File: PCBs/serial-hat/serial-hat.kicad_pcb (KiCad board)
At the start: 2 copper layers, 65 x 56 mm, 21 parts, among them J1 CTS/RTS3, J2 TX/RX3, J3 CTS/RTS2, J4 TX/RX2, J5 UART3, J6 UART2, J7 Conn_02x20_Odd_Even, U1 MAX3232, U2 MAX3232

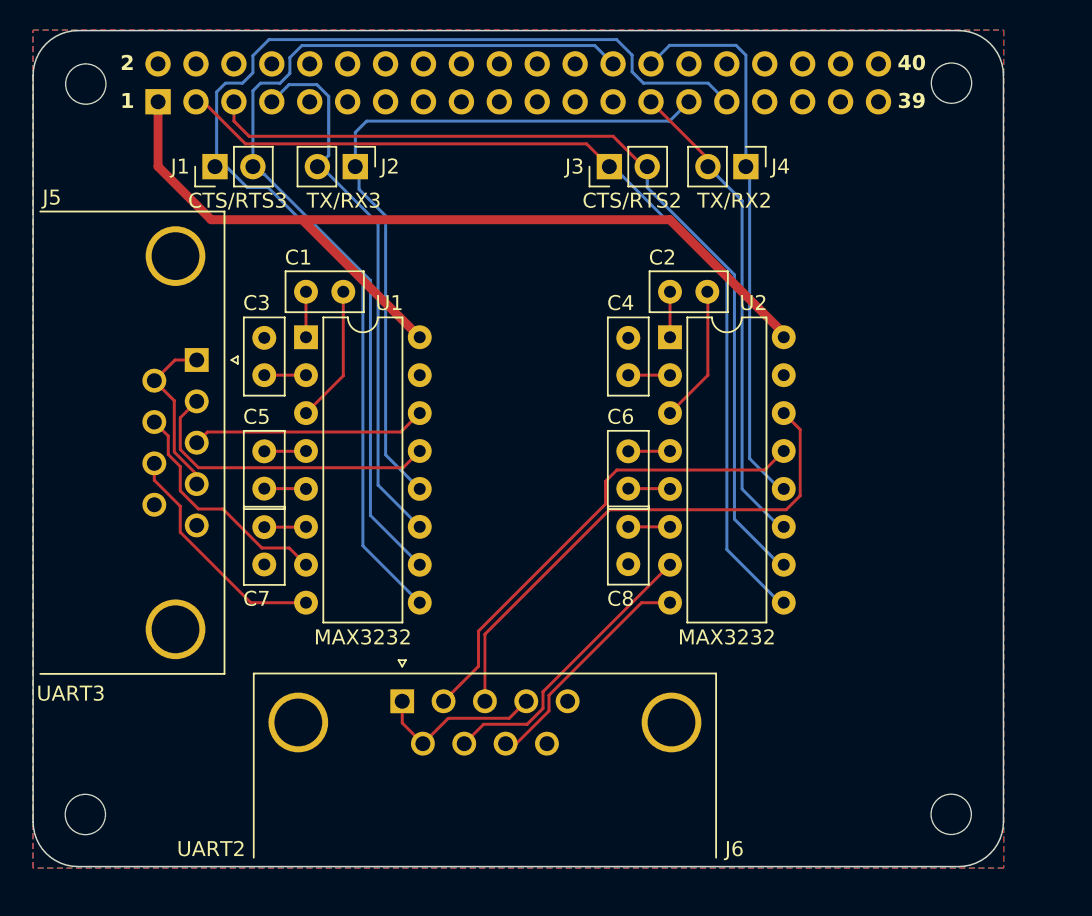
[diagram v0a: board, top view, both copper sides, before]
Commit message: Rework for single MAX3232
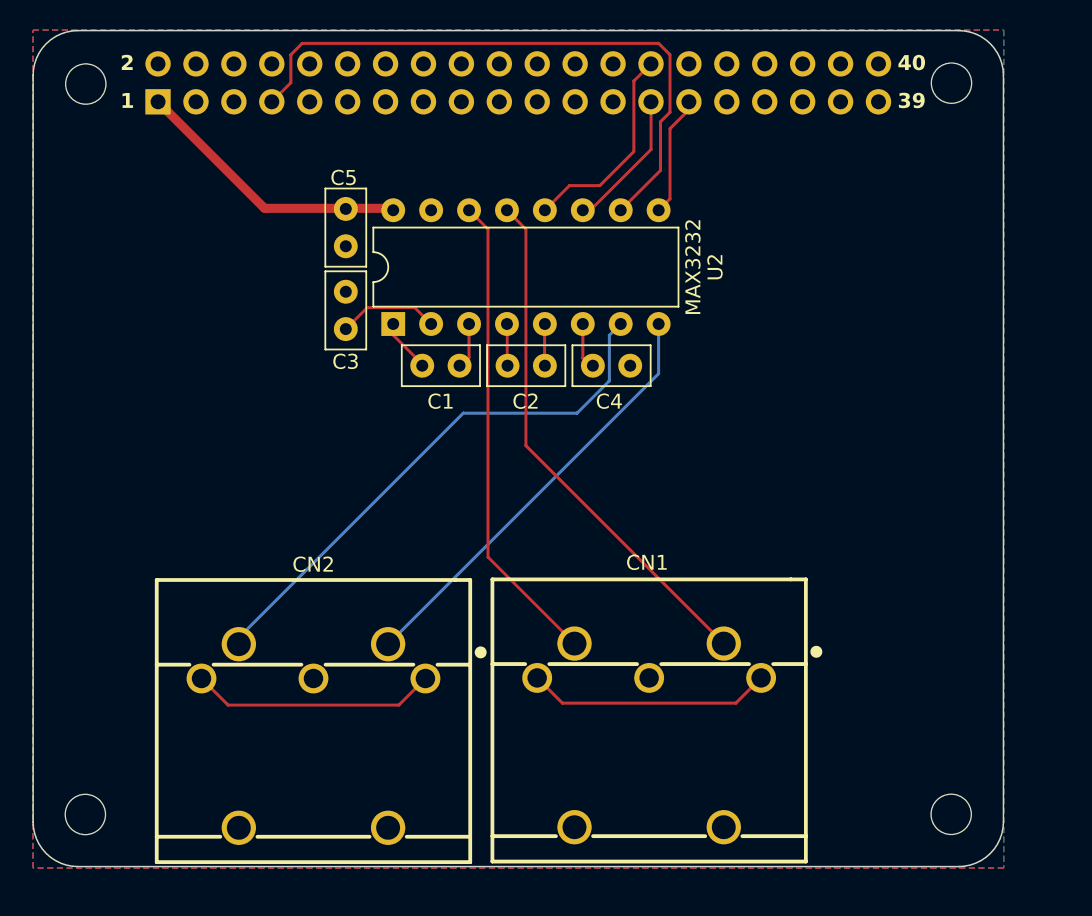
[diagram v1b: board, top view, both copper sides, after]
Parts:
- removed C6, C7, C8: 100nF, Capacitor_THT:C_Disc_D5.0mm_W2.5mm_P2.50mm
- removed J1: CTS/RTS3, Connector_PinHeader_2.54mm:PinHeader_1x02_P2.54mm_Vertical
- removed J2: TX/RX3, Connector_PinHeader_2.54mm:PinHeader_1x02_P2.54mm_Vertical
- removed J3: CTS/RTS2, Connector_PinHeader_2.54mm:PinHeader_1x02_P2.54mm_Vertical
- removed J4: TX/RX2, Connector_PinHeader_2.54mm:PinHeader_1x02_P2.54mm_Vertical
- removed J5: UART3, Connector_Dsub:DSUB-9_Male_Horizontal_P2.77x2.84mm_EdgePinOffset7.70mm_Housed_MountingHolesOffset9.12mm
- removed J6: UART2, Connector_Dsub:DSUB-9_Male_Horizontal_P2.77x2.84mm_EdgePinOffset7.70mm_Housed_MountingHolesOffset9.12mm
- removed U1: MAX3232, Package_DIP:DIP-16_W7.62mm
- added CN1: Modem port, DIN5:CONN-TH_DIN-504-M10, F.Cu at (164.0, 99.8)
- added CN2: Printer port, DIN5:CONN-TH_DIN-504-M10, F.Cu at (141.5, 99.9)
- J7: value Conn_02x20_Odd_Even -> Rpi headers
- moved U2 18.6 mm to (146.8, 72.3), turned to 90 degrees
- moved C5 17.1 mm to (143.6, 64.6)
- moved C2 12.0 mm to (154.5, 75.1)
- moved C1 9.23 mm to (148.8, 75.1)
- moved C3 6.27 mm to (143.6, 72.6)
- moved C4 2.46 mm to (160.2, 75.1), turned to 0 degrees
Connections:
- C1 pad 1: Net-(U1-C1+) -> Net-(U2-C1+)
- C1 pad 2: Net-(U1-C1-) -> Net-(U2-C1-)
- C2 pad 1: Net-(U2-C1+) -> Net-(U2-C2+)
- C2 pad 2: Net-(U2-C1-) -> Net-(U2-C2-)
- C3 pad 1: Net-(U1-VS+) -> Net-(U2-VS+)
- C4 pad 1: Net-(U2-VS+) -> Net-(U2-VS-)
- C5 pad 1: Net-(U1-C2+) -> 3.3V
- C5 pad 2: Net-(U1-C2-) -> GND
- J7 pad 26: RTS1_GPIO7 -> unconnected-(J7-Pin_26-Pad26)
- J7 pad 3: CTS0_out_GPIO2 -> unconnected-(J7-Pin_3-Pad3)
- J7 pad 31: CTS1_out_GPIO6 -> unconnected-(J7-Pin_31-Pad31)
- J7 pad 5: RTS0_GPIO3 -> unconnected-(J7-Pin_5-Pad5)
- U2 pad 10: RTS0_GPIO3 -> TX1_out_GPIO4
- U2 pad 13: RX0_in -> TX0_in
- U2 pad 14: TX0_in -> RX0_in
- U2 pad 7: RTS0_in -> RX1_in
- U2 pad 8: CTS0_in -> TX1_in
- U2 pad 9: CTS0_out_GPIO2 -> RX1_OUT_GPIO5
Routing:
- net CTS1_out_GPIO6: track 79.5 -> 0.00 mm
- net CTS0_out_GPIO2: track 63.1 -> 0.00 mm
- net RTS1_GPIO7: track 62.3 -> 0.00 mm
- net RTS0_GPIO3: track 60.3 -> 0.00 mm
- net 3.3V: track 62.4 -> 18.8 mm
- net RX1_OUT_GPIO5: track 48.5 -> 8.10 mm
- net RX0_OUT_GPIO1: track 36.8 -> 13.9 mm
- net TX0_out_GPIO0: track 31.5 -> 9.46 mm
- net RTS0_in: track 19.4 -> 0.00 mm
- net Net-(CN2-Pad1): track 0.00 -> 16.5 mm
- net Net-(CN1-Pad1): track 0.00 -> 16.4 mm
- net RX1_in: track 20.7 -> 36.5 mm
- net RTS1_in: track 15.8 -> 0.00 mm
- net CTS1_in: track 15.7 -> 0.00 mm
- net CTS0_in: track 15.5 -> 0.00 mm
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
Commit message: Test with Max232 + shifter
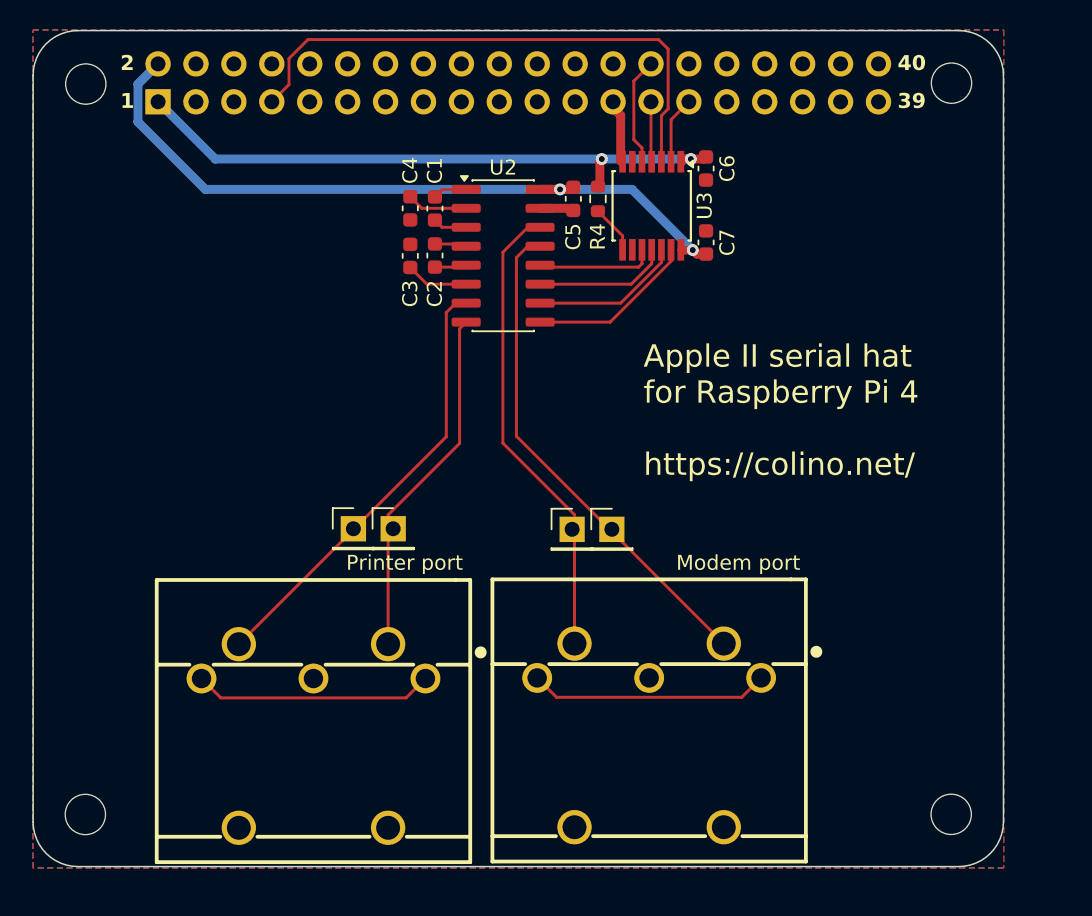
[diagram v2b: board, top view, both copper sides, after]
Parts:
- added C6: 100n, Capacitor_SMD:C_0603_1608Metric, F.Cu at (167.8, 61.8)
- added C7: 100n, Capacitor_SMD:C_0603_1608Metric, F.Cu at (167.8, 66.8)
- added R4: 10k, Resistor_SMD:R_0603_1608Metric, F.Cu at (160.5, 63.9)
- added REF**: PinHeader_1x01_P2.54mm_Vertical, Connector_PinHeader_2.54mm:PinHeader_1x01_P2.54mm_Vertical, F.Cu at (144.1, 86.0)
- added REF**: PinHeader_1x01_P2.54mm_Vertical, Connector_PinHeader_2.54mm:PinHeader_1x01_P2.54mm_Vertical, F.Cu at (146.8, 86.0)
- added REF**: PinHeader_1x01_P2.54mm_Vertical, Connector_PinHeader_2.54mm:PinHeader_1x01_P2.54mm_Vertical, F.Cu at (158.8, 86.0)
- added REF**: PinHeader_1x01_P2.54mm_Vertical, Connector_PinHeader_2.54mm:PinHeader_1x01_P2.54mm_Vertical, F.Cu at (161.5, 86.0)
- added U3: TXB0104PWR level shifter, Package_SO:TSSOP-14-1EP_4.4x5mm_P0.65mm, F.Cu at (164.1, 64.3)
- C1, C2, C3, C4, C5: value 100nF -> 1µf; footprint Capacitor_THT:C_Disc_D5.0mm_W2.5mm_P2.50mm -> Capacitor_SMD:C_0603_1608Metric
- U2: value MAX3232 -> MAX232; footprint Package_DIP:DIP-16_W7.62mm -> Package_SO:SOIC-16_3.9x9.9mm_P1.27mm
- moved C5 15.3 mm to (158.9, 63.9)
- moved C4 14.3 mm to (148.0, 67.7), turned to 90 degrees
- moved C1 10.6 mm to (149.6, 64.5), turned to -90 degrees
- moved C3 9.17 mm to (148.0, 64.5), turned to -90 degrees
- moved C2 8.84 mm to (149.6, 67.7), turned to -90 degrees
- moved U2 8.67 mm to (154.2, 67.7), turned to 0 degrees
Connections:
- net RX0_in renamed RX0_a2
- net RX1_in renamed RX1_a2
- net TX0_in renamed TX0_a2
- net TX1_in renamed TX1_a2
- C5 pad 1: 3.3V -> 5V
- J7 pad 2: unconnected-(J7-Pin_2-Pad2) -> 5V
- J7 pad 27: TX0_out_GPIO0 -> TX0_pi
- J7 pad 28: RX0_OUT_GPIO1 -> RX0_pi
- J7 pad 29: RX1_OUT_GPIO5 -> RX1_pi
- J7 pad 7: TX1_out_GPIO4 -> TX1_pi
- U2 pad 10: TX1_out_GPIO4 -> TX1_5V
- U2 pad 11: TX0_out_GPIO0 -> TX0_5V
- U2 pad 12: RX0_OUT_GPIO1 -> RX0_5V
- U2 pad 16: 3.3V -> 5V
- U2 pad 9: RX1_OUT_GPIO5 -> RX1_5V
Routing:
- net 5V: track 0.00 -> 49.2 mm, vias 0 -> 2
- net TX1_out_GPIO4: track 41.5 -> 0.00 mm
- net TX1_pi: track 0.00 -> 37.3 mm
- net 3.3V: track 18.8 -> 41.0 mm, vias 0 -> 2
- net RX0_OUT_GPIO1: track 13.9 -> 0.00 mm
- net RX1_5V: track 0.00 -> 11.2 mm
- net TX1_5V: track 0.00 -> 10.1 mm
- net TX0_out_GPIO0: track 9.46 -> 0.00 mm
- net TX0_5V: track 0.00 -> 8.97 mm
- net RX1_OUT_GPIO5: track 8.10 -> 0.00 mm
- net RX0_5V: track 0.00 -> 7.90 mm
- net RX0_pi: track 0.00 -> 7.26 mm
- net RX1_a2: track 36.5 -> 29.6 mm
- net GND: track 0.00 -> 6.53 mm
- net TX1_a2: track 29.0 -> 23.7 mm
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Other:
- board text added: "Apple II serial hat for Raspberry Pi 4 https://colino.net/"

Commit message: Back to MAX3232
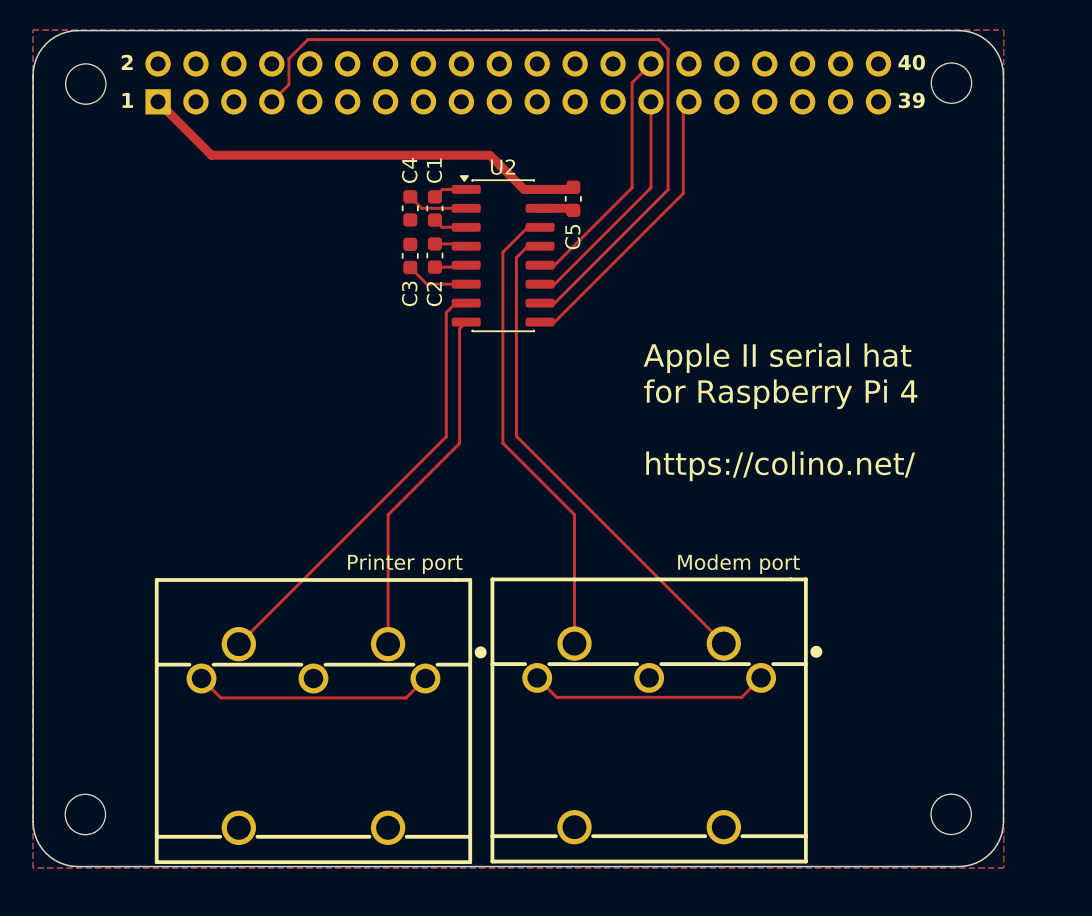
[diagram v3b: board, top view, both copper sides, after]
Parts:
- removed C6, C7: 100n, Capacitor_SMD:C_0603_1608Metric
- removed R4: 10k, Resistor_SMD:R_0603_1608Metric
- removed the REF** at (144.1, 86.0)
- removed the REF** at (146.8, 86.0)
- removed the REF** at (158.8, 86.0)
- removed the REF** at (161.5, 86.0)
- removed U3: TXB0104PWR level shifter, Package_SO:TSSOP-14-1EP_4.4x5mm_P0.65mm
- C1, C2, C3, C4, C5: value 1µf -> 100nF
- U2: value MAX232 -> MAX3232
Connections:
- net RX0_a2 renamed RX0_in
- net RX1_a2 renamed RX1_in
- net TX0_a2 renamed TX0_in
- net TX1_a2 renamed TX1_in
- C5 pad 1: 5V -> 3.3V
- J7 pad 2: 5V -> unconnected-(J7-Pin_2-Pad2)
- J7 pad 27: TX0_pi -> TX0_out_GPIO0
- J7 pad 28: RX0_pi -> RX0_OUT_GPIO1
- J7 pad 29: RX1_pi -> RX1_OUT_GPIO5
- J7 pad 7: TX1_pi -> TX1_out_GPIO4
- U2 pad 10: TX1_5V -> TX1_out_GPIO4
- U2 pad 11: TX0_5V -> TX0_out_GPIO0
- U2 pad 12: RX0_5V -> RX0_OUT_GPIO1
- U2 pad 16: 5V -> 3.3V
- U2 pad 9: RX1_5V -> RX1_OUT_GPIO5
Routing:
- net TX1_out_GPIO4: track 0.00 -> 50.7 mm
- net 5V: track 49.2 -> 0.00 mm, vias 2 -> 0
- net TX1_pi: track 37.3 -> 0.00 mm
- net RX1_OUT_GPIO5: track 0.00 -> 19.5 mm
- net RX0_OUT_GPIO1: track 0.00 -> 17.1 mm
- net TX0_out_GPIO0: track 0.00 -> 15.9 mm
- net RX1_5V: track 11.2 -> 0.00 mm
- net 3.3V: track 41.0 -> 30.3 mm, vias 2 -> 0
- net TX1_5V: track 10.1 -> 0.00 mm
- net TX0_5V: track 8.97 -> 0.00 mm
- net RX0_5V: track 7.90 -> 0.00 mm
- net RX0_pi: track 7.26 -> 0.00 mm
- net RX1_pi: track 4.51 -> 0.00 mm
- net GND: track 6.53 -> 2.28 mm
- net TX0_pi: track 4.04 -> 0.00 mm
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
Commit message: WIP - CISD
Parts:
- added R1: 3.3k, Resistor_SMD:R_0603_1608Metric, F.Cu at (155.1, 77.7)
- added R2: 3.3k, Resistor_SMD:R_0603_1608Metric, F.Cu at (151.3, 77.7)
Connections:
- U2 pad 13: TX0_in -> Net-(U2-R1IN)
- U2 pad 8: TX1_in -> Net-(U2-R2IN)
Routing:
- net TX0_in: track 33.5 -> 20.9 mm
- net Net-(U2-R1IN): track 0.00 -> 11.0 mm
- net TX1_in: track 23.7 -> 17.1 mm
- net Net-(U2-R2IN): track 0.00 -> 4.95 mm
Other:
- board text added: "Apple II serial hat for Raspberry Pi 4/5 https://colino.net/"
- board text added: "Pi4: modem: ttyAMA2 printer: ttyAMA3 Pi5: modem: ttyAMA1 printer: ttyAMA2"
- board text removed: "Apple II serial hat for Raspberry Pi 4 https://colino.net/"

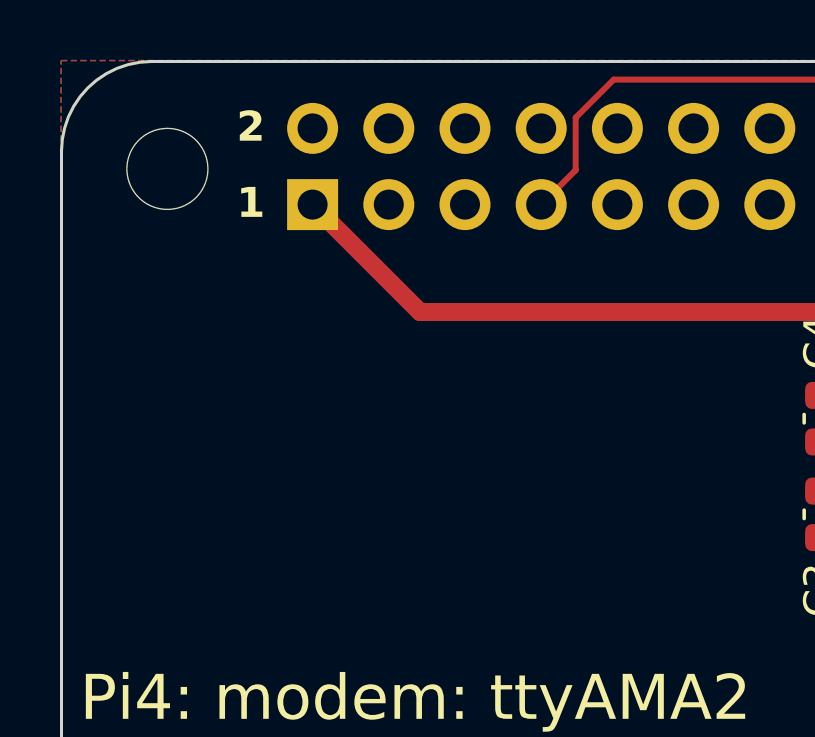
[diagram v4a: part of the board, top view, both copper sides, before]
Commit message: Add fan headers
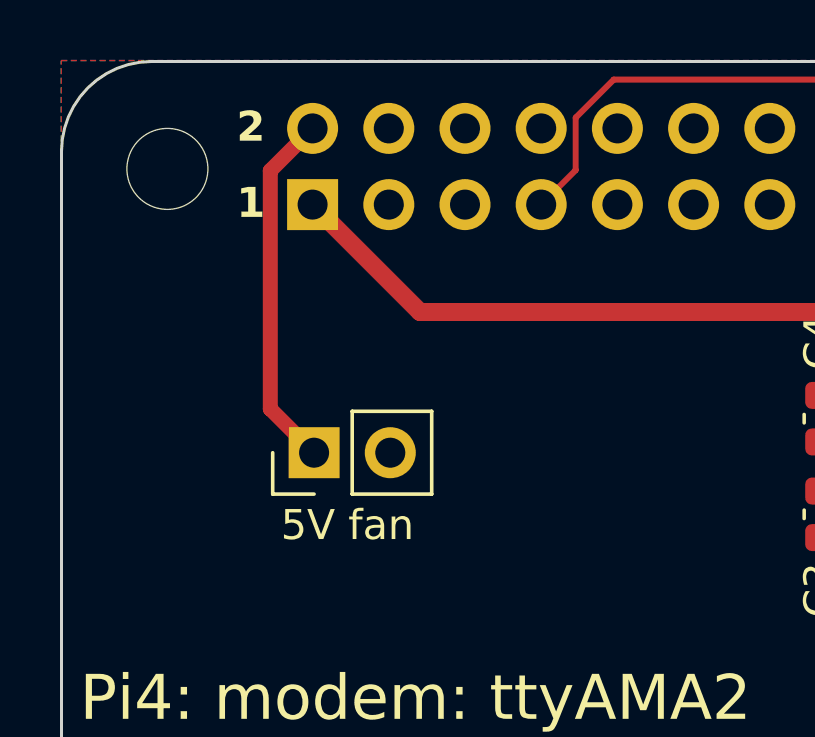
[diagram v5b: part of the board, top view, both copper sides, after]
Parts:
- added J1: Conn_01x02_Pin, Connector_PinHeader_2.54mm:PinHeader_1x02_P2.54mm_Vertical, F.Cu at (131.1, 65.7)
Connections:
- J7 pad 2: unconnected-(J7-Pin_2-Pad2) -> 5V
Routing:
- net 5V: track 0.00 -> 12.0 mm
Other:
- board text added: "5V fan"

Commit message: CISD ready
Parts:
- removed R1, R2: 3.3k, Resistor_SMD:R_0603_1608Metric
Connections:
- U2 pad 13: Net-(U2-R1IN) -> TX0_in
- U2 pad 8: Net-(U2-R2IN) -> TX1_in
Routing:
- net TX0_in: track 20.9 -> 33.5 mm
- net Net-(U2-R1IN): track 11.0 -> 0.00 mm
- net TX1_in: track 17.1 -> 23.7 mm
- net Net-(U2-R2IN): track 4.95 -> 0.00 mm
